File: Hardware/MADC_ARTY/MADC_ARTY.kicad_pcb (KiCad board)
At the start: 4 copper layers, 139 x 70 mm, 243 parts, among them J1 Conn_01x01, J2 Conn_01x01, J3 Conn_01x02, J4 71764-0012, J5 71764-0012, Q1 JFE2140D, Q10 MMBT6429, Q11 MMBF4392, Q12 MMBT6429, Q13 MMBT6429, Q2 MMBT6429, Q3 MMBT6429, Q4 MMBF4392, Q5 MMBT6429, Q6 MMBT6429, Q7 SiS443DN, Q8 JFE2140D, Q9 MMBT6429, U1 OPA2192, U10 AQY212G3HS, U11 AD8422ARMZ, U12 ADG419BRM, U13 ADG419BRM, U14 LT5400-6, U15 LT5400-2, U16 DG419xY, U17 DG211BDQ, U18 OPA2192, U19 LT5400-1, U2 OPA4192IPW, U20 OPA140, U21 OPA192, U22 LM311, U23 OPA2192, U24 ADR1399KEZ, U25 ADG419BRM, U26 ADG419BRM, U27 OPA2192, U28 OPA4192IPW, U3 TSR3-2450N, U4 ADP5070AREZ, U5 ADP7142ARDZ-3.3, U6 ADP7142ARDZ, U7 ADP7182ACPZN, U8 ADP7182ACPZN, U9 AQY212G3HS

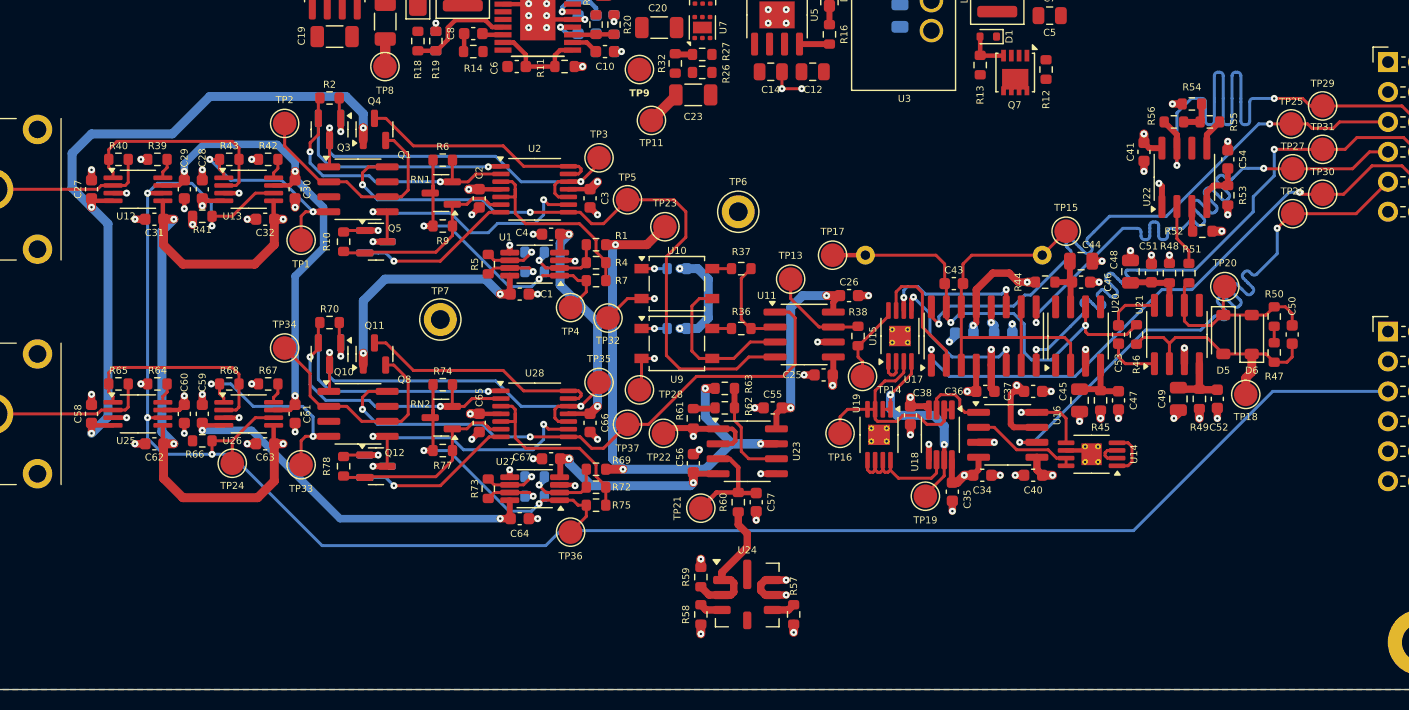
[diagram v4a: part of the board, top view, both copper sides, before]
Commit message: MADC module send to production
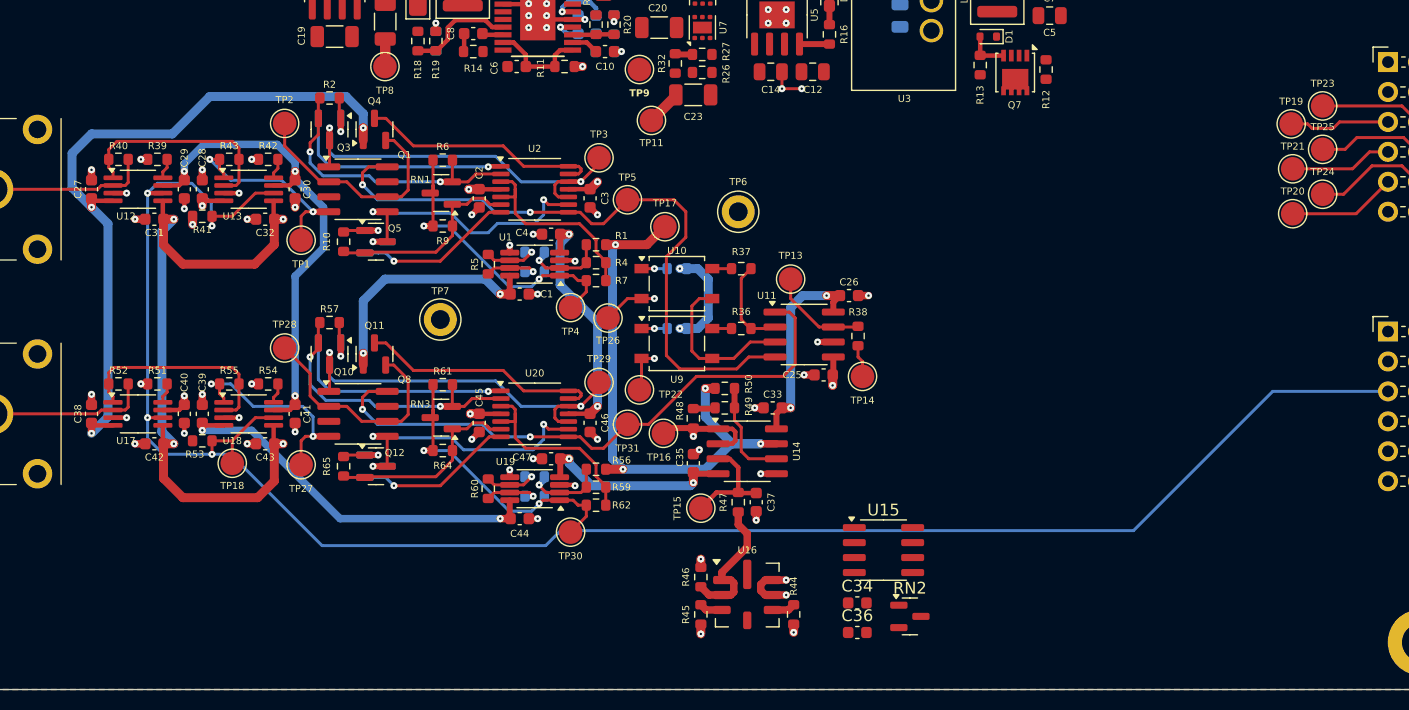
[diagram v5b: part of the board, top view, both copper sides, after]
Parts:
- removed the C33 at (184.3, 79.8)
- removed the C35 at (183.3, 93.2)
- removed the C37 at (190.1, 84.7)
- removed the C38 at (179.7, 86.7)
- removed the C39 at (187.6, 79.8)
- removed the C40 at (190.1, 91.8)
- removed the C41 at (199.5, 64.4)
- removed the C42 at (175.9, 73.2)
- removed the C43 at (183.4, 75.6)
- removed the C44 at (194.2, 73.7)
- removed the C45 at (194.1, 85.5)
- removed the C46 at (194.2, 75.4)
- removed the C47 at (197.4, 85.5)
- removed C48, C49: 10u/35V, Capacitor_SMD:C_0805_2012Metric
- removed C50: 33p, Capacitor_SMD:C_0603_1608Metric
- removed C51, C52: 1u/35V, Capacitor_SMD:C_0603_1608Metric
- removed C53: DNP, Capacitor_SMD:C_0603_1608Metric
- removed C54: 0.1u, Capacitor_SMD:C_0603_1608Metric
- removed D5, D6: BAV21W, Diode_SMD:D_SOD-123
- removed the R44 at (191.1, 75.4)
- removed the R45 at (195.8, 85.5)
- removed the R46 at (198.9, 79.9)
- removed the R47 at (210.6, 81.4)
- removed the R48 at (201.7, 74.7)
- removed the R49 at (204.2, 85.3)
- removed the R50 at (210.6, 78.4)
- removed the R51 at (203.3, 74.7)
- removed the R52 at (204.5, 71.1)
- removed the R53 at (206.6, 68.1)
- removed the R54 at (203.6, 60.3)
- removed the R55 at (205.1, 61.8)
- removed the R56 at (202.1, 61.8)
- removed the TP15 at (192.9, 71.1)
- removed the TP16 at (173.7, 88.3)
- removed the TP17 at (173.1, 73.2)
- removed the TP18 at (208.2, 85.0)
- removed the TP19 at (181.0, 93.6)
- removed the TP20 at (206.4, 75.8)
- removed the U14 at (195.1, 90.0)
- removed the U16 at (188.0, 88.4)
- removed the U17 at (185.9, 80.0)
- removed the U18 at (182.2, 88.4)
- removed the U19 at (177.0, 88.4)
- removed the U20 at (193.9, 80.0)
- removed U21: OPA192, Package_SO:SOIC-8_3.9x4.9mm_P1.27mm
- removed U22: LM311, Package_SO:SOIC-8_3.9x4.9mm_P1.27mm
- added RN2: MPMT1002AT1, Package_TO_SOT_SMD:SOT-23, F.Cu at (179.7, 103.8)
- R46: renamed from R59; value 12k/1%/125mW -> 1k8/1%/125mW
- U15: value LT5400-2 -> OPA2192; footprint Package_SO:MSOP-8-1EP_3x3mm_P0.65mm_EP1.73x1.85mm_ThermalVias -> Package_SO:SOIC-8_3.9x4.9mm_P1.27mm
- moved C36 23.2 mm to (175.2, 105.2)
- moved U15 18.2 mm to (177.4, 98.2), turned to 0 degrees
- moved C34 15.2 mm to (175.2, 102.7)
- renumbered C55 to C33, C56 to C35, C57 to C37, C58 to C38, C59 to C39, C60 to C40, C61 to C41, C62 to C42, C63 to C43, C64 to C44, C65 to C45, C66 to C46, C67 to C47, R57 to R44, R58 to R45, R60 to R47, R61 to R48, R62 to R49, R63 to R50, R64 to R51, R65 to R52, R66 to R53, R67 to R54, R68 to R55, R69 to R56, R70 to R57, R71 to R58, R72 to R59, R73 to R60, R74 to R61, R75 to R62, R76 to R63, R77 to R64, R78 to R65, RN2 to RN3, TP21 to TP15, TP22 to TP16, TP23 to TP17, TP24 to TP18, TP25 to TP19, TP26 to TP20, TP27 to TP21, TP28 to TP22, TP29 to TP23, TP30 to TP24, TP31 to TP25, TP32 to TP26, TP33 to TP27, TP34 to TP28, TP35 to TP29, TP36 to TP30, TP37 to TP31, U23 to U14, U24 to U16, U25 to U17, U26 to U18, U27 to U19, U28 to U20
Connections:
- net /Block Diagram/ADC/AD_COMP renamed /Block Diagram/PMOD/AD_COMP
- net /Block Diagram/ADC/FGPA_AD_ID renamed /Block Diagram/PMOD/FGPA_AD_ID
- net /Block Diagram/ADC/FGPA_AD_IIN renamed /Block Diagram/PMOD/FGPA_AD_IIN
- net /Block Diagram/ADC/FGPA_AD_IRN renamed /Block Diagram/PMOD/FGPA_AD_IRN
- net /Block Diagram/ADC/FGPA_AD_IRP renamed /Block Diagram/PMOD/FGPA_AD_IRP
- net /Block Diagram/ADC/FPGA_SW_VRH renamed /Block Diagram/PMOD/FPGA_SW_VRH
- Q1 pad 2: Net-(Q4-S) -> Net-(Q4-D)
- Q1 pad 6: Net-(Q4-S) -> Net-(Q4-D)
- Q11 pad 1: +18V -> Net-(Q11-D)
- Q11 pad 2: Net-(Q11-S) -> +18V
- Q4 pad 1: +18V -> Net-(Q4-D)
- Q4 pad 2: Net-(Q4-S) -> +18V
- Q8 pad 2: Net-(Q11-S) -> Net-(Q11-D)
- Q8 pad 6: Net-(Q11-S) -> Net-(Q11-D)
- R38 pad 2: /Block Diagram/ADC/ADIN -> /Block Diagram/Gain/ANALOG
- TP14 pad 1: /Block Diagram/ADC/ADIN -> /Block Diagram/Gain/ANALOG
- TP2 pad 1: Net-(Q4-S) -> Net-(Q4-D)
- TP28 pad 1: Net-(Q11-S) -> Net-(Q11-D)
- U15 pad 1: Net-(U15-Pad1) -> +7V
- U15 pad 2: Net-(U15-Pad1) -> Net-(U15A--)
- U15 pad 3: /Block Diagram/ADC/VREF- -> GND
- U15 pad 4: /Block Diagram/ADC/VREF+ -> -18V
- U15 pad 5: Net-(U15-Pad5) -> GND
- U15 pad 6: Net-(U15-Pad6) -> Net-(U15B--)
- U15 pad 7: Net-(U15-Pad7) -> Net-(U15B--)
- U15 pad 8: /Block Diagram/ADC/ADIN -> +18V
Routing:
- net -14V: track 94.7 -> 4.81 mm, vias 4 -> 1
- net +3.3V: track 260.7 -> 181.7 mm, vias 11 -> 6
- net /Block Diagram/PMOD/FGPA_AD_IIN: track 52.1 -> 9.65 mm, vias 2 -> 0
- net /Block Diagram/PMOD/AD_COMP: track 50.9 -> 8.65 mm, vias 2 -> 0
- net /Block Diagram/PMOD/FGPA_AD_IRN: track 51.3 -> 9.00 mm, vias 2 -> 0
- net /Block Diagram/PMOD/FPGA_SW_VRH: track 51.5 -> 9.29 mm, vias 2 -> 0
- net /Block Diagram/PMOD/FGPA_AD_ID: track 50.8 -> 8.60 mm, vias 2 -> 0
- net /Block Diagram/PMOD/FGPA_AD_IRP: track 50.8 -> 8.68 mm, vias 2 -> 0
- net Net-(C42-Pad1): track 37.9 -> 0.00 mm, vias 2 -> 0
- net Net-(U20--): track 34.8 -> 0.00 mm
- net -7V: track 44.2 -> 10.5 mm, vias 2 -> 1
- net -18V: track 241.2 -> 210.9 mm, vias 14 -> 11
- net +18V: track 330.3 -> 302.3 mm, vias 17 -> 13
- net GND: track 74.4 -> 47.2 mm, vias 80 -> 57
- net Net-(D5-A): track 21.4 -> 0.00 mm
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
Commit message: PCB and schematic
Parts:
- added C48: 0.1u, Capacitor_SMD:C_0603_1608Metric, F.Cu at (202.4, 66.4)
- added C49: 0.1u, Capacitor_SMD:C_0603_1608Metric, F.Cu at (202.4, 72.0)
- added R66: 0, Resistor_SMD:R_0603_1608Metric, F.Cu at (186.7, 79.9)
- added R67: 0, Resistor_SMD:R_0603_1608Metric, F.Cu at (186.7, 82.2)
- added R68: 0, Resistor_SMD:R_0603_1608Metric, F.Cu at (182.1, 74.9)
- added R69: 0, Resistor_SMD:R_0603_1608Metric, F.Cu at (184.7, 74.9)
- added R70: 0, Resistor_SMD:R_0603_1608Metric, F.Cu at (216.5, 56.8)
- added R71: 0, Resistor_SMD:R_0603_1608Metric, F.Cu at (205.2, 70.2)
- added R72: 1k, Resistor_SMD:R_0603_1608Metric, F.Cu at (205.2, 67.2)
- added R73: 0, Resistor_SMD:R_0603_1608Metric, F.Cu at (199.8, 69.1)
- added U21: MADC, MADC:MADC, F.Cu at (187.8, 74.3)
- added U22: SN74LVC1T45DBV, Package_TO_SOT_SMD:SOT-23-6, F.Cu at (202.4, 69.2)
- Q11, Q4: value MMBF4392 -> MMBF4392LT1G
- moved C34 17.1 mm to (180.1, 86.2), turned to 180 degrees
- moved RN2 16.7 mm to (172.3, 88.8), turned to -90 degrees
- moved C36 12.0 mm to (176.5, 93.2)
- moved U15 8.43 mm to (178.3, 89.8)
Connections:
- net /Block Diagram/Gain/ANALOG renamed /Block Diagram/ADC/AD_IN
- net /Block Diagram/PMOD/AD_COMP renamed /Block Diagram/ADC/AD_CMP
- net /Block Diagram/PMOD/FGPA_AD_ID renamed /Block Diagram/ADC/AD_ID
- net /Block Diagram/PMOD/FGPA_AD_IIN renamed /Block Diagram/ADC/AD_IIN
- net /Block Diagram/PMOD/FGPA_AD_IRN renamed /Block Diagram/ADC/AD_IRN
- net /Block Diagram/PMOD/FGPA_AD_IRP renamed /Block Diagram/ADC/AD_IRP
- net /Block Diagram/PMOD/FPGA_SW_VRH renamed /Block Diagram/ADC/SW_VRH
- net /Block Diagram/Power/EN1 renamed Net-(U4-EN1)
- J4 pad 1: unconnected-(J4-Pin_1-Pad1) -> +3.3VP
- J4 pad 2: unconnected-(J4-Pin_2-Pad2) -> +3.3VP
- J5 pad 1: unconnected-(J5-Pin_1-Pad1) -> +3.3VP
- J5 pad 2: unconnected-(J5-Pin_2-Pad2) -> +3.3VP
- Q1 pad 2: Net-(Q4-D) -> Net-(Q4-S)
- Q1 pad 6: Net-(Q4-D) -> Net-(Q4-S)
- Q11 pad 1: Net-(Q11-D) -> +18V
- Q11 pad 2: +18V -> Net-(Q11-S)
- Q4 pad 1: Net-(Q4-D) -> +18V
- Q4 pad 2: +18V -> Net-(Q4-S)
- Q8 pad 2: Net-(Q11-D) -> Net-(Q11-S)
- Q8 pad 6: Net-(Q11-D) -> Net-(Q11-S)
- TP2 pad 1: Net-(Q4-D) -> Net-(Q4-S)
- TP28 pad 1: Net-(Q11-D) -> Net-(Q11-S)
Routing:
- net +18V: track 302.3 -> 264.4 mm
- net Net-(Q4-S): track 0.00 -> 19.8 mm
- net Net-(Q11-S): track 0.00 -> 19.8 mm
- net -7V: track 10.5 -> 21.3 mm, vias 1 -> 2
- net /Block Diagram/Auto Zero/AZ_CTR: track 162.4 -> 170.4 mm
- net Net-(U15A--): track 0.00 -> 3.72 mm
- net +7V: track 0.00 -> 2.56 mm
- net -18V: track 210.9 -> 212.5 mm
- net -14V: track 4.81 -> 3.66 mm

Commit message: BOM
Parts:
- added C26: 0.1u, Capacitor_SMD:C_0603_1608Metric, F.Cu at (167.6, 72.0)
- added C28: 0.1u, Capacitor_SMD:C_0603_1608Metric, F.Cu at (176.7, 69.5)
- added D2: 1N4148W, Diode_SMD:D_SOD-123, F.Cu at (189.2, 65.0)
- added Q8: MMBT3904VL, Package_TO_SOT_SMD:SOT-23, F.Cu at (194.1, 62.6)
- added R16: 100k, Resistor_SMD:R_0603_1608Metric, F.Cu at (189.9, 62.9)
- added R35: 0, Resistor_SMD:R_0603_1608Metric, F.Cu at (166.1, 67.2)
- added R36: 0, Resistor_SMD:R_0603_1608Metric, F.Cu at (166.1, 65.4)
- added R37: 0, Resistor_SMD:R_0603_1608Metric, F.Cu at (165.7, 77.0)
- added R38: 0, Resistor_SMD:R_0603_1608Metric, F.Cu at (165.7, 81.8)
- added R43: 0, Resistor_SMD:R_0603_1608Metric, F.Cu at (176.7, 72.5)
- added R80: 6k2, Resistor_SMD:R_0603_1608Metric, B.Cu at (162.7, 57.1)
- added RN2: LT5400BCMS8E-1#PBF, Package_SO:MSOP-8-1EP_3x3mm_P0.65mm_EP1.73x1.85mm, F.Cu at (172.2, 66.3)
- added TP13: TestPoint, TestPoint:TestPoint_Pad_D2.0mm, F.Cu at (168.8, 74.9)
- added TP14: TestPoint, TestPoint:TestPoint_Pad_D2.0mm, F.Cu at (165.0, 71.4)
- added TP15: TestPoint, TestPoint:TestPoint_Pad_D2.0mm, F.Cu at (177.2, 64.8)
- added U11: ADA4522-1ARZ, Package_SO:SOIC-8_3.9x4.9mm_P1.27mm, F.Cu at (172.2, 70.9)
- C11: moved to F.Cu
- D1: value DZ2S100X0L -> BZX84C10LT1G; footprint Diode_SMD:D_SOD-523 -> Package_TO_SOT_SMD:SOT-23
- J3: value Conn_01x02 -> 1715721; footprint TerminalBlock_Phoenix:TerminalBlock_Phoenix_MPT-0,5-2-2.54_1x02_P2.54mm_Horizontal -> TerminalBlock_Phoenix:TerminalBlock_Phoenix_MKDS-1,5-2_1x02_P5.00mm_Horizontal
- Q10: renamed from Q9; value MMBT6429 -> MMBT6429LT1G
- Q11: renamed from Q10; value MMBT6429 -> MMBT6429LT1G
- Q13: renamed from Q12; value MMBT6429 -> MMBT6429LT1G
- Q14: renamed from Q13; value MMBT6429 -> MMBT6429LT1G
- Q2, Q3, Q5, Q6: value MMBT6429 -> MMBT6429LT1G
- U1: value OPA2192 -> OPA2192IDGKT
- U17: renamed from U14; value OPA2192 -> OPA2192IDGKT
- U18: renamed from U15; value OPA2192 -> OPA2192IDGKT
- U22: renamed from U19; value OPA2192 -> OPA2192IDGKT
- moved TP6 32.2 mm to (184.3, 95.4)
- moved R56 19.4 mm to (202.9, 86.5), turned to 180 degrees
- moved C35 17.3 mm to (203.7, 83.7), turned to 90 degrees
- moved R55 17.1 mm to (199.9, 86.5), turned to 0 degrees
- moved U16 14.5 mm to (200.9, 83.7), turned to 180 degrees
- moved D1 13.8 mm to (197.6, 62.6), turned to -90 degrees
- moved C36 12.7 mm to (198.1, 83.9), turned to 90 degrees
- moved R54 12.1 mm to (201.0, 81.2), turned to 180 degrees
- moved TP16 10.0 mm to (179.3, 77.3)
- moved R13 9.82 mm to (195.1, 59.7), turned to 0 degrees
- moved R50 9.71 mm to (193.8, 86.5)
- moved R52 9.42 mm to (189.6, 80.6)
- moved R51 9.20 mm to (193.8, 88.0)
- moved U15 9.12 mm to (194.9, 80.0)
- moved R53 8.83 mm to (191.4, 80.6)
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- renumbered C26 to C27, C27 to C29, C28 to C30, C29 to C31, C30 to C32, C31 to C33, C32 to C34, C48 to C35, C49 to C36, C33 to C37, C34 to C38, C35 to C39, C36 to C40, C37 to C41, C38 to C42, C39 to C43, C40 to C44, C41 to C45, C42 to C46, C43 to C47, C44 to C48, C45 to C49, C46 to C50, C47 to C51, D2 to D3, D3 to D4, D4 to D5, Q11 to Q12, Q8 to Q9, R16 to R17, R17 to R18, R18 to R19, R19 to R20, R20 to R21, R21 to R22, R22 to R23, R23 to R24, R24 to R25, R25 to R26, R26 to R27, R27 to R28, R28 to R29, R29 to R30, R30 to R31, R31 to R32, R32 to R33, R33 to R34, R34 to R39, R35 to R40, R36 to R41, R37 to R42, R38 to R44, R39 to R45, R40 to R46, R41 to R47, R42 to R48, R43 to R49, R66 to R50, R67 to R51, R68 to R52, R69 to R53, R73 to R54, R71 to R55, R72 to R56, R44 to R57, R45 to R58, R46 to R59, R47 to R60, R48 to R61, R49 to R62, R50 to R63, R70 to R64, R51 to R65, R52 to R66, R53 to R67, R54 to R68, R55 to R69, R56 to R70, R57 to R71, R58 to R72, R59 to R73, R60 to R74, R61 to R75, R62 to R76, R63 to R77, R64 to R78, R65 to R79, RN2 to RN3, RN3 to RN4, TP13 to TP16, TP14 to TP17, TP15 to TP18, TP16 to TP19, TP17 to TP20, TP18 to TP21, TP19 to TP22, TP20 to TP23, TP21 to TP24, TP22 to TP25, TP23 to TP26, TP24 to TP27, TP25 to TP28, TP26 to TP29, TP27 to TP30, TP28 to TP31, TP29 to TP32, TP30 to TP33, TP31 to TP34, U11 to U12, U12 to U13, U13 to U14, U21 to U15, U22 to U16, U16 to U19, U17 to U20, U18 to U21, U20 to U23
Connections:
- D1 pad 1: +24V -> Net-(D1-A)
- D1 pad 2: Net-(D1-A) -> unconnected-(D1-NC-Pad2)
- R27 pad 1: GND -> Net-(R27-Pad1)
- U12 pad 1: /Block Diagram/Analog Channels1/OUT -> Net-(U12--)
- U12 pad 4: /Block Diagram/Analog Channels/OUT -> Net-(U12-+)
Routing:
- net /Block Diagram/Auto Zero/AZ_CTR: track 170.4 -> 54.1 mm
- net /Block Diagram/Analog Channels1/OUT: track 50.2 -> 35.5 mm
- net /Block Diagram/ADC/AD_IIN: track 9.65 -> 0.00 mm
- net /Block Diagram/ADC/SW_VRH: track 9.29 -> 0.08 mm
- net Net-(U4-FB1): track 9.14 -> 0.00 mm
- net /Block Diagram/ADC/AD_IRN: track 9.00 -> 0.00 mm
- net /Block Diagram/ADC/AD_IRP: track 8.68 -> 0.00 mm
- net /Block Diagram/ADC/AD_CMP: track 8.65 -> 0.00 mm
- net /Block Diagram/ADC/AD_ID: track 8.60 -> 0.00 mm
- net /Block Diagram/Analog Channels/OUT: track 56.4 -> 47.9 mm
- net Net-(U4-EN1): track 8.47 -> 0.00 mm
- net Net-(R41-Pad2): track 7.89 -> 0.18 mm
- net GND: track 47.2 -> 40.1 mm, vias 57 -> 56
- net Net-(U10-Pad3): track 13.7 -> 7.80 mm
- net Net-(U4-VREG): track 5.13 -> 0.00 mm, vias 1 -> 0
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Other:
- board size 139 x 70 mm -> 133 x 70 mm
